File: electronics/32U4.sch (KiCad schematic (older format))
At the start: 10 parts, among them J1 Input 5v, U1 Pro Micro 32U4 USB

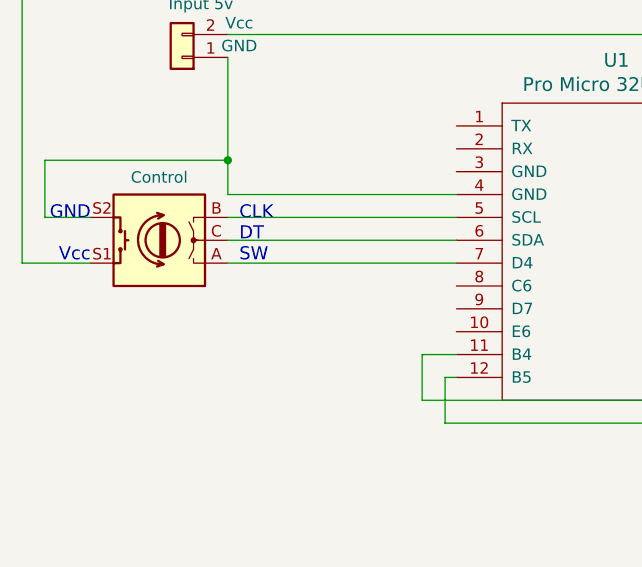
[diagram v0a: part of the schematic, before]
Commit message: Added second rotary encoder
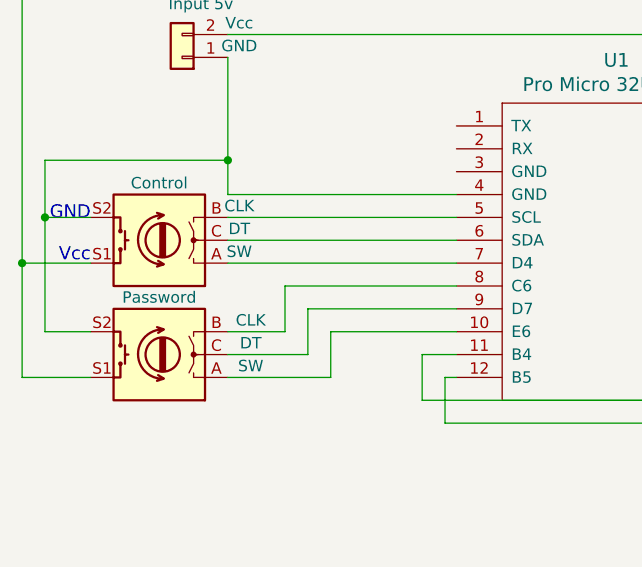
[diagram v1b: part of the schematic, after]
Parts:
- added Password: Rotary_Encoder_Switch, symbol Device:Rotary_Encoder_Switch
- Control: CLK (none) -> CLK; DT (none) -> DT; SW (none) -> SW
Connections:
- net at U1.10 (E6): now also Password.A
- net at 1.8".7 (Pin_7), Control.S1, U1.21 (VCC): now also Password.S1
- net at Control.S2, J1.1 (Pin_1), U1.4 (GND): now also Password.S2
- net at U1.8 (C6): now also Password.B
- net at U1.9 (D7): now also Password.C
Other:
- note removed: "CLK\nDT\nSW"
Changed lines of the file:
@@
 U 1 1 5E7EB2C9
 P 1300 2850
-F 0 "Control" H 1300 2575 50  0000 C CNN
+F 0 "Control" H 1300 2600 50  0000 C CNN
 F 1 "Rotary_Encoder_Switch" H 1300 3126 50  0001 C CNN
 F 2 "" H 1150 3010 50  0001 C CNN
 F 3 "~" H 1300 3125 50  0001 C CNN
+F 4 "CLK" H 950 2700 50  0000 C CNN "CLK"
+F 5 "DT" H 950 2800 50  0000 C CNN "DT"
+F 6 "SW" H 950 2900 50  0000 C CNN "SW"
 	1    1300 2850
 	-1   0    0    1
 $EndComp
-Text Notes 1650 2950 0    57   ~ 0
-CLK\nDT\nSW
 Wire Wire Line
 	1600 2750 2600 2750
@@
 Wire Wire Line
 	4150 1950 4150 2350
+$Comp
+L Device:Rotary_Encoder_Switch Password
+U 1 1 5EA37447
+P 1300 3350
+F 0 "Password" H 1300 3100 50  0000 C CNN
+F 1 "Rotary_Encoder_Switch" H 1300 3626 50  0001 C CNN
+F 2 "" H 1150 3510 50  0001 C CNN
+F 3 "~" H 1300 3625 50  0001 C CNN
+F 4 "CLK" H 900 3200 50  0000 C CNN "CLK"
+F 5 "DT" H 900 3300 50  0000 C CNN "DT"
+F 6 "SW" H 900 3400 50  0000 C CNN "SW"
+	1    1300 3350
+	-1   0    0    1
+$EndComp
+Wire Wire Line
+	1000 3450 700  3450
+Wire Wire Line
+	700  3450 700  2950
+Connection ~ 700  2950
+Wire Wire Line
+	800  2750 800  3250
+Wire Wire Line
+	800  3250 1000 3250
+Connection ~ 800  2750
+Wire Wire Line
+	1600 3250 1850 3250
+Wire Wire Line
+	1850 3250 1850 3050
+Wire Wire Line
+	1850 3050 2600 3050
+Wire Wire Line
+	1600 3350 1950 3350
+Wire Wire Line
+	1950 3350 1950 3150
+Wire Wire Line
+	1950 3150 2600 3150
+Wire Wire Line
+	1600 3450 2050 3450
+Wire Wire Line
+	2050 3450 2050 3250
+Wire Wire Line
+	2050 3250 2600 3250
 $EndSCHEMATC

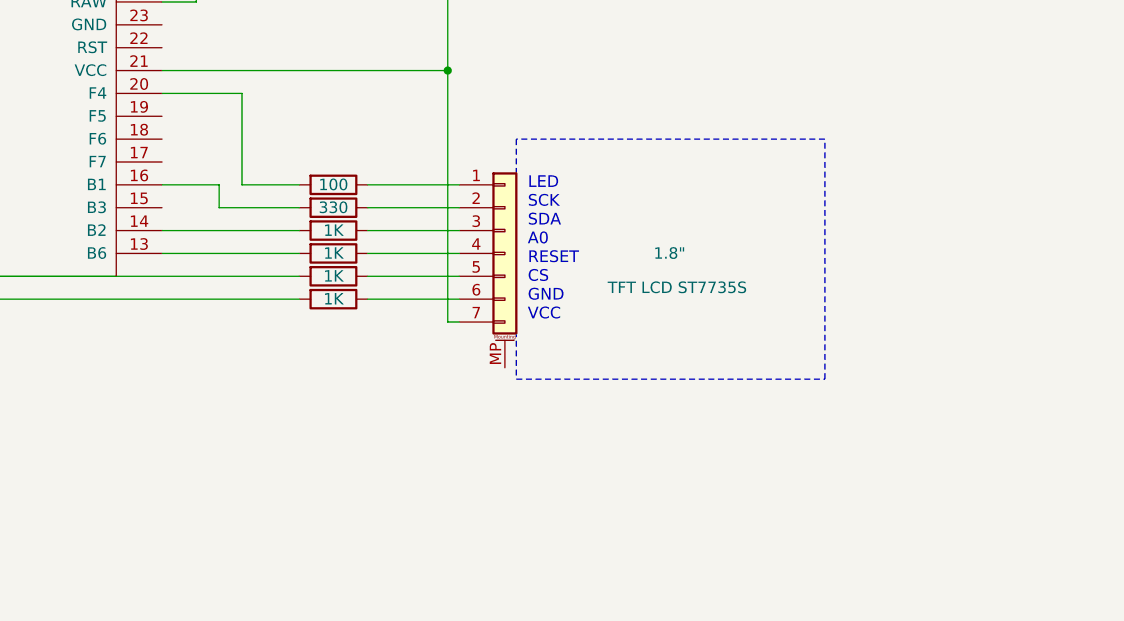
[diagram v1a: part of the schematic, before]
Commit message: Added SD Card for password manager
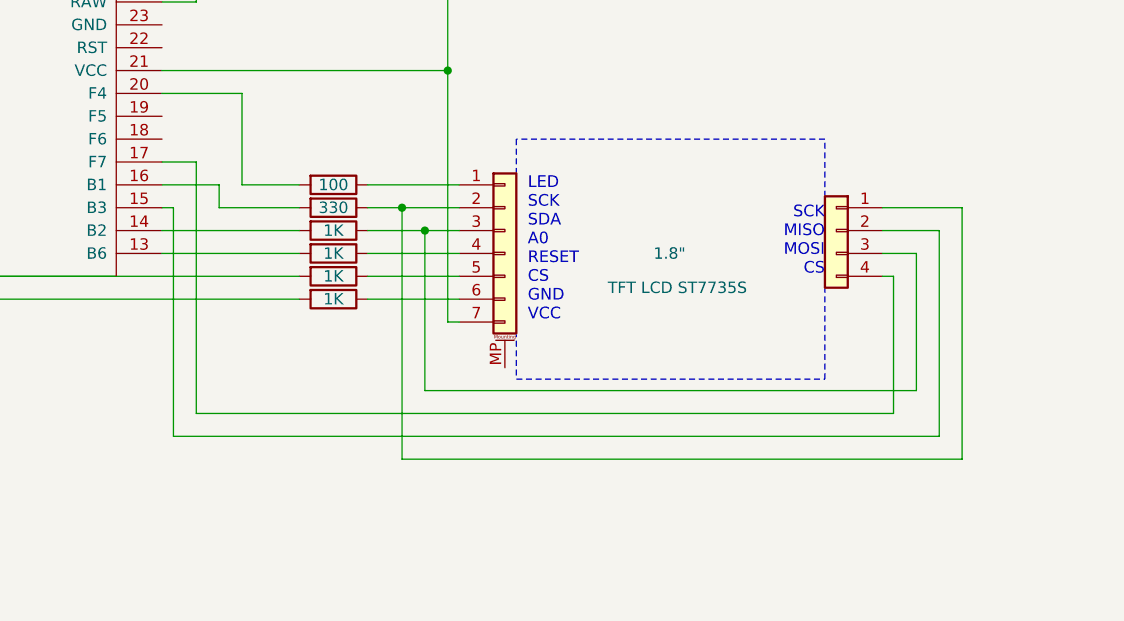
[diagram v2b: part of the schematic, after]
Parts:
- added J?: Conn_01x04, symbol Connector_Generic:Conn_01x04
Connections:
- net at U1.15 (B3): now also J?.2 (Pin_2)
- net at U1.17 (F7): now also J?.4 (Pin_4)
- net at 1.8".2 (Pin_2), R?.1: now also J?.1 (Pin_1)
- net at 1.8".3 (Pin_3), R?.1: now also J?.3 (Pin_3)
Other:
- note added: "SCK\nMISO\nMOSI\nCS"
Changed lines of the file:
@@
 	4000 3150 4250 3150
 Wire Wire Line
-	4900 3250 5300 3250
-Wire Wire Line
-	4900 3350 5300 3350
+	4900 3250 5050 3250
+Wire Wire Line
+	4900 3350 5150 3350
 Wire Wire Line
 	4900 3450 5300 3450
@@
 Wire Wire Line
 	2050 3250 2600 3250
+$Comp
+L Connector_Generic:Conn_01x04 J?
+U 1 1 5EA4FC54
+P 6950 3350
+F 0 "J?" H 6868 2925 50  0001 C CNN
+F 1 "Conn_01x04" H 6868 3016 50  0001 C CNN
+F 2 "" H 6950 3350 50  0001 C CNN
+F 3 "~" H 6950 3350 50  0001 C CNN
+	1    6950 3350
+	-1   0    0    -1
+$EndComp
+Text Notes 6900 3550 2    51   ~ 0
+SCK\nMISO\nMOSI\nCS
+Wire Wire Line
+	5150 3350 5150 4050
+Wire Wire Line
+	5150 4050 7300 4050
+Wire Wire Line
+	7300 4050 7300 3450
+Wire Wire Line
+	7300 3450 7150 3450
+Connection ~ 5150 3350
+Wire Wire Line
+	5150 3350 5300 3350
+Wire Wire Line
+	4000 3050 4150 3050
+Wire Wire Line
+	4150 3050 4150 4150
+Wire Wire Line
+	4150 4150 7200 4150
+Wire Wire Line
+	7200 4150 7200 3550
+Wire Wire Line
+	7200 3550 7150 3550
+Wire Wire Line
+	7150 3350 7400 3350
+Wire Wire Line
+	7400 3350 7400 4250
+Wire Wire Line
+	7400 4250 4050 4250
+Wire Wire Line
+	4050 4250 4050 3250
+Wire Wire Line
+	4050 3250 4000 3250
+Wire Wire Line
+	7150 3250 7500 3250
+Wire Wire Line
+	7500 3250 7500 4350
+Wire Wire Line
+	7500 4350 5050 4350
+Wire Wire Line
+	5050 4350 5050 3250
+Connection ~ 5050 3250
+Wire Wire Line
+	5050 3250 5300 3250
 $EndSCHEMATC

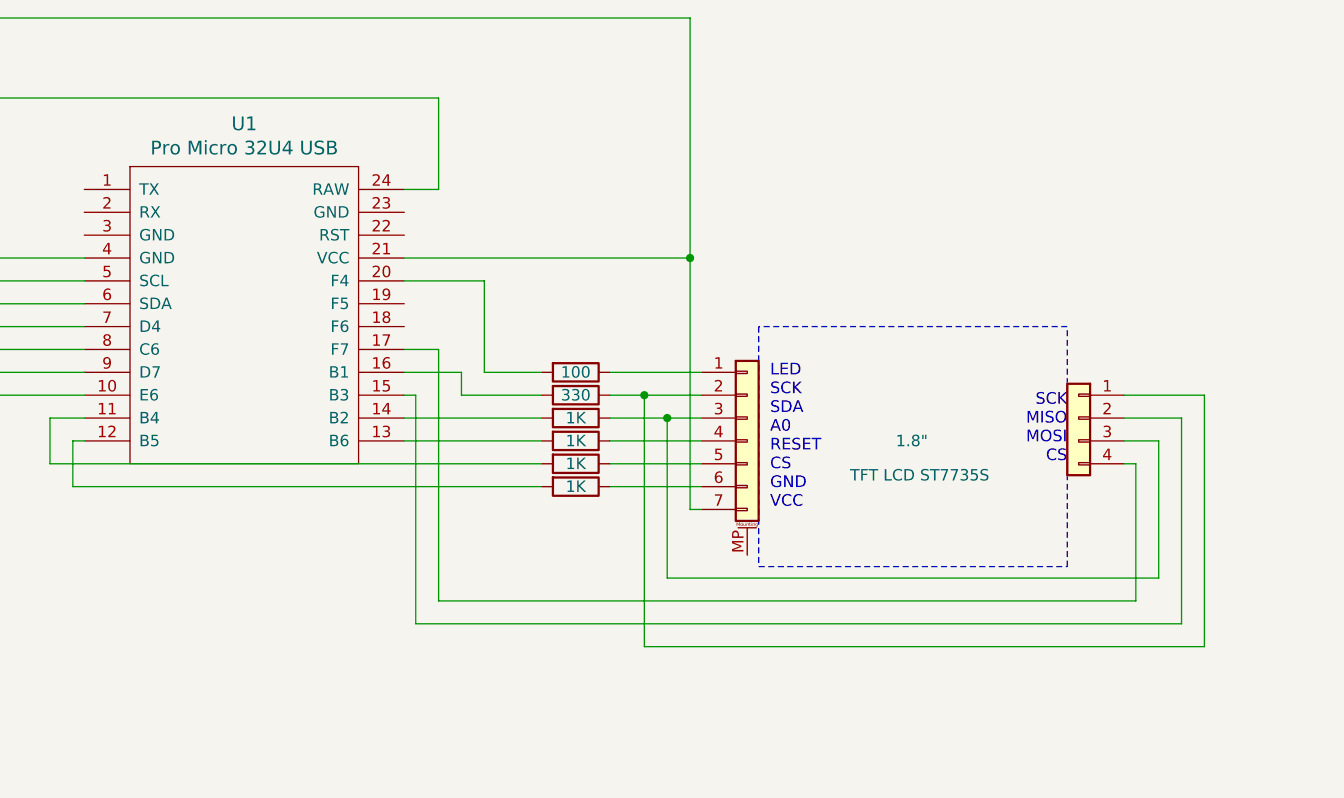
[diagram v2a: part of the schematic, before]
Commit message: SD Card added, 16U4 Labels added
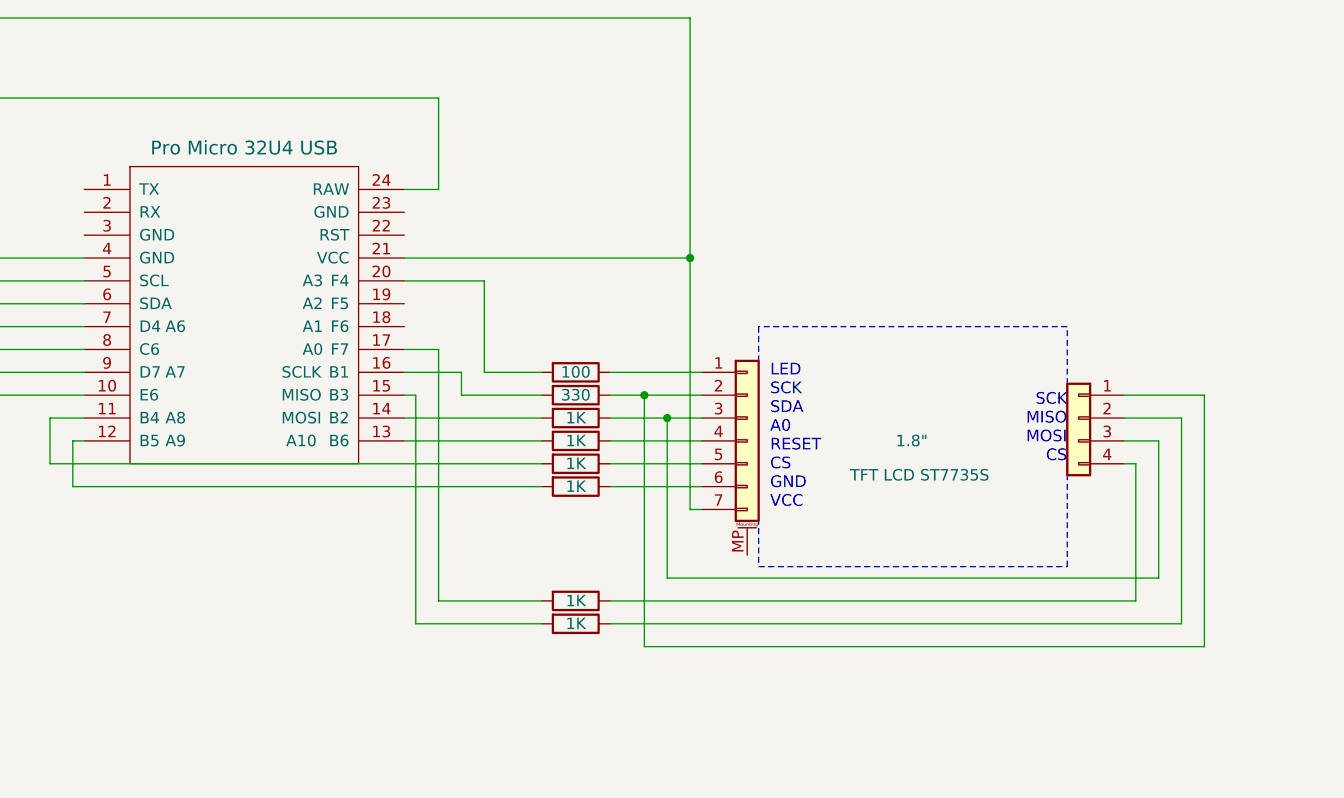
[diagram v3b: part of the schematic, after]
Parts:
- added R? (x2): 1K, symbol Device:R
- U1: A0 (none) -> A0; A1 (none) -> A1; A10 (none) -> A10; A2 (none) -> A2; A3 (none) -> A3; A6 (none) -> A6; A7 (none) -> A7; A8 (none) -> A8; A9 (none) -> A9; MISO (none) -> MISO; MOSI (none) -> MOSI; SCLK (none) -> SCLK
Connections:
- net at U1.15 (B3): now also R?.2; no longer J?.2 (Pin_2)
- net at U1.17 (F7): now also R?.2; no longer J?.4 (Pin_4)
- new net: J?.2 (Pin_2), R?.1
- new net: J?.4 (Pin_4), R?.1
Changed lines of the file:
@@
 U 1 1 5E755F83
 P 3300 3100
-F 0 "U1" H 3300 4137 60  0000 C CNN
+F 0 "U1" H 3300 4137 60  0001 C CNN
 F 1 "Pro Micro 32U4 USB" H 3300 4031 60  0000 C CNN
 F 2 "" H 3400 2050 60  0000 C CNN
 F 3 "" H 3400 2050 60  0000 C CNN
+F 4 "A0" H 3600 3150 50  0000 C CNN "A0"
+F 5 "A1" H 3600 3250 50  0000 C CNN "A1"
+F 6 "A2" H 3600 3350 50  0000 C CNN "A2"
+F 7 "A3" H 3600 3450 50  0000 C CNN "A3"
+F 8 "SCLK" H 3550 3050 50  0000 C CNN "SCLK"
+F 9 "MISO" H 3550 2950 50  0000 C CNN "MISO"
+F 10 "MOSI" H 3550 2850 50  0000 C CNN "MOSI"
+F 11 "A10" H 3550 2750 50  0000 C CNN "A10"
+F 12 "A6" H 3000 3250 50  0000 C CNN "A6"
+F 13 "A7" H 3000 3050 50  0000 C CNN "A7"
+F 14 "A8" H 3000 2850 50  0000 C CNN "A8"
+F 15 "A9" H 3000 2750 50  0000 C CNN "A9"
 	1    3300 3100
 	1    0    0    -1
@@
 	4150 3050 4150 4150
 Wire Wire Line
-	4150 4150 7200 4150
+	4150 4150 4600 4150
 Wire Wire Line
 	7200 4150 7200 3550
@@
 	7400 3350 7400 4250
 Wire Wire Line
-	7400 4250 4050 4250
+	7400 4250 4900 4250
 Wire Wire Line
 	4050 4250 4050 3250
@@
 Wire Wire Line
 	5050 3250 5300 3250
+$Comp
+L Device:R R?
+U 1 1 5EA68409
+P 4750 4150
+F 0 "R?" V 4543 4150 50  0001 C CNN
+F 1 "1K" V 4750 4150 50  0000 C CNN
+F 2 "" V 4680 4150 50  0001 C CNN
+F 3 "~" H 4750 4150 50  0001 C CNN
+	1    4750 4150
+	0    1    1    0
+$EndComp
+$Comp
+L Device:R R?
+U 1 1 5EA68789
+P 4750 4250
+F 0 "R?" V 4543 4250 50  0001 C CNN
+F 1 "1K" V 4750 4250 50  0000 C CNN
+F 2 "" V 4680 4250 50  0001 C CNN
+F 3 "~" H 4750 4250 50  0001 C CNN
+	1    4750 4250
+	0    1    1    0
+$EndComp
+Wire Wire Line
+	4900 4150 7200 4150
+Wire Wire Line
+	4050 4250 4600 4250
 $EndSCHEMATC
